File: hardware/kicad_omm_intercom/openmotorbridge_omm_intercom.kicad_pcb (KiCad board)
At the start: 2 copper layers, 60 x 30 mm, 19 parts, among them J1 TYPE-C-31-M-12_IP67, SW1 Power_MFB, SW2 Mesh_Group, SW3 Vol_Plus, SW4 Vol_Minus, U1 ESP32-C6-MINI-1U, U2 BQ24075RGTR, U3 XC6206P332MR, U4 ES8388, U5 ESP32-PICO-V3-02

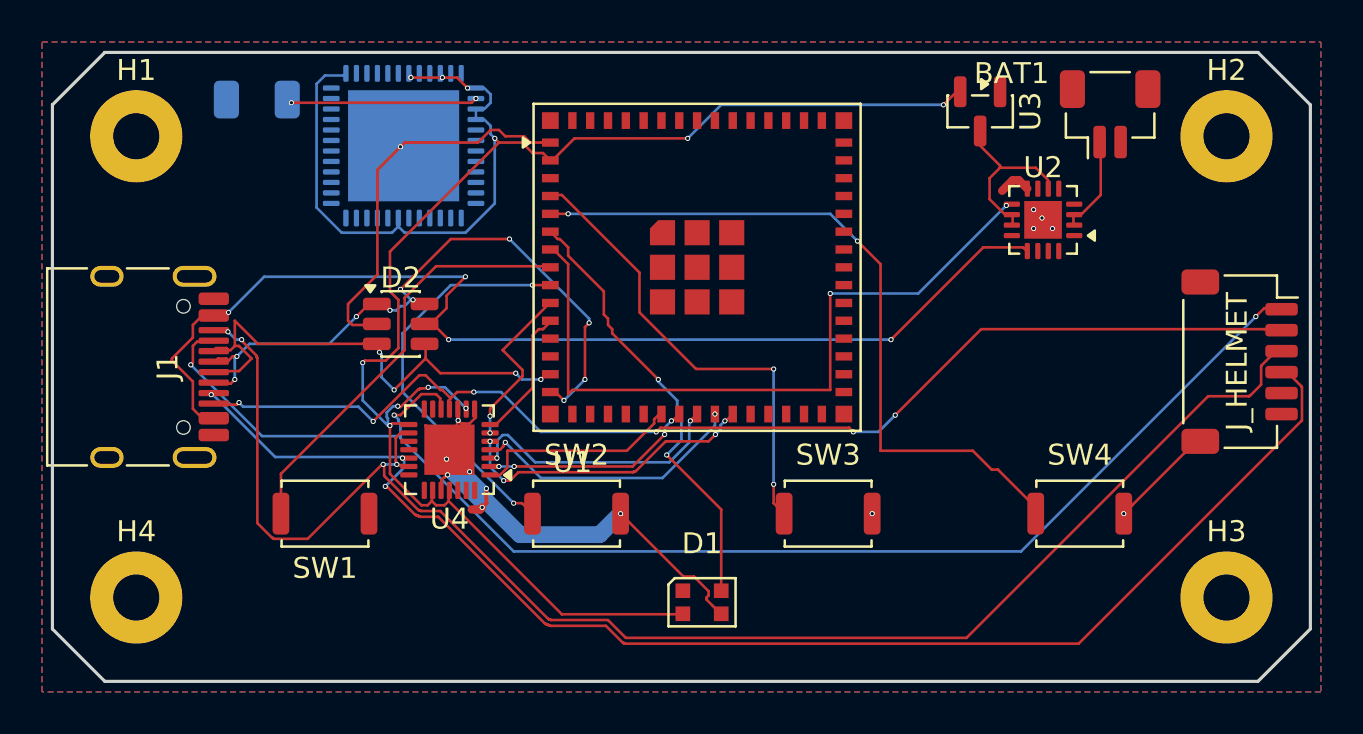
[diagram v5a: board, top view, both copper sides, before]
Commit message: hardware(omm): rotate J_HELMET by 180° inward, update CAD cutouts, CPL, gerbers, and docs
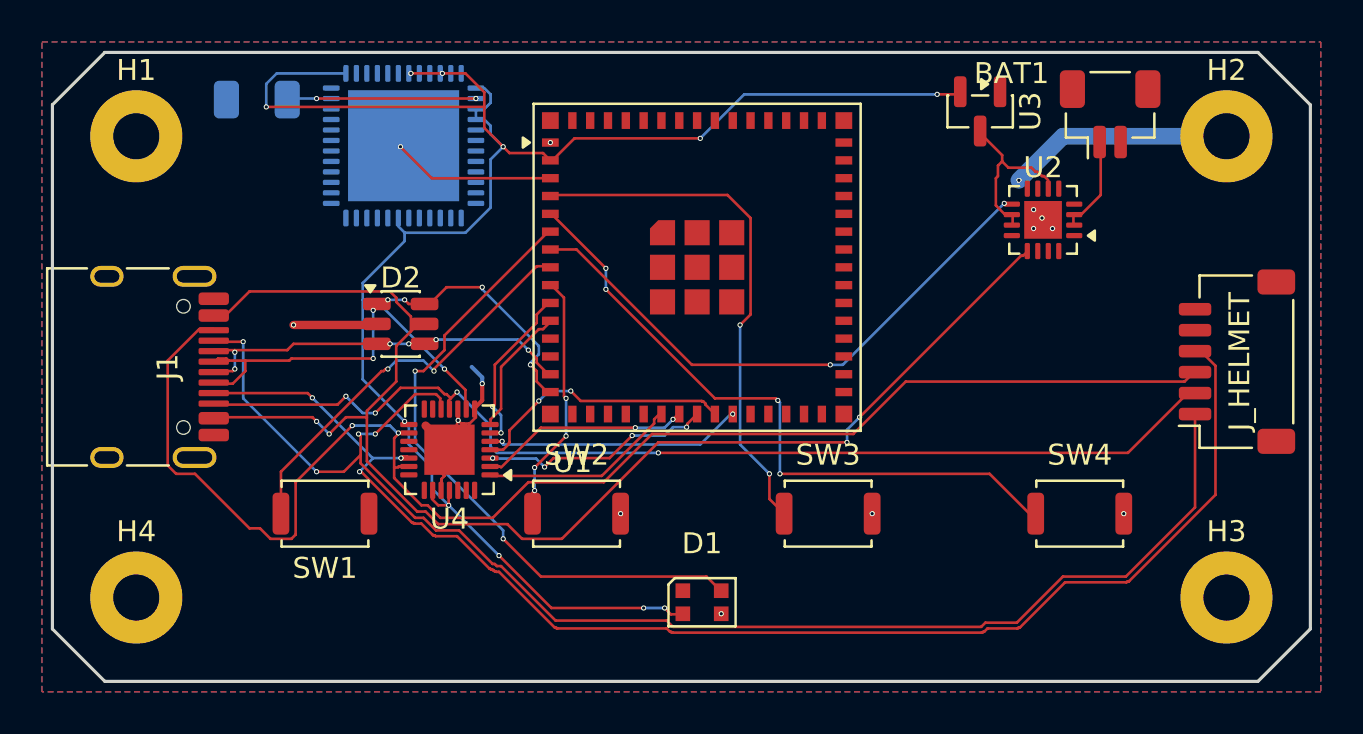
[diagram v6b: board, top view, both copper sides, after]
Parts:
- moved J_HELMET 0.12 mm to (126.5, 99.8), turned to 90 degrees
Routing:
- net GND: track 57.3 -> 38.3 mm
- net VBUS_5V: track 51.7 -> 65.2 mm
- net WS2812_DATA: track 20.9 -> 30.6 mm
- net BTN_MESH: track 19.5 -> 11.9 mm, vias 2 -> 4
- net CHG_STAT: track 34.5 -> 27.5 mm
- net USB_DP: track 29.4 -> 23.9 mm, vias 10 -> 6
- net USB_DN: track 23.5 -> 18.4 mm, vias 4 -> 6
- net AGND_SPK: track 73.7 -> 68.7 mm, vias 4 -> 2
- net HP_OUT_R: track 56.3 -> 51.4 mm, vias 6 -> 4
- net BTN_VOL_UP: track 22.3 -> 25.1 mm
- net BTN_VOL_DOWN: track 34.1 -> 31.7 mm, vias 2 -> 4
- net I2S_DIN: track 14.5 -> 12.5 mm, vias 4 -> 2
- net I2S_WS: track 12.5 -> 10.9 mm, vias 2 -> 4
- net HP_OUT_L: track 66.9 -> 68.1 mm, vias 3 -> 4
- net VCC_3V3: track 94.7 -> 95.8 mm, vias 11 -> 12
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
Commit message: feat(hw): finalize PCB lineup routing, sync PCBA 03 cartridge with J_PROG header and DTM12 schematics
- PCBA 01 (Central Box): Remediate net routing, DTM12 hierarchical schematic synchronization, 100% routed, 0 DRC errors.
- PCBA 03 (Smart Modular Cartridge): Position and route J_PROG 4-pin SMD programming header on F.Cu at (108.0, 89.61), synchronize CPL and schematic, 100% routed, 0 DRC errors.
- PCBA 05 (Universal Front Node): Preconnect and routing verified, 100% routed, 0 DRC errors.
- PCBA 07 (LoRa Smart-Keyfob): Routing and DRC verified, 100% routed, 0 DRC errors.
- PCBA 08 (Radar 2.0 Sub-MCU & Wings): Sub-MCU routing and HF isolation verified, 100% routed, 0 DRC errors.
- PCBA 10 (OMM 446 PMR/DMR Intercom): KiCad DRC verified, 100% routed, 0 DRC errors.
- Firmware: Align configuration headers across front_node and smart_cartridge.
- Tools: Add comprehensive preflight PCBA audit suite tools/audit_pcbas_preflight.py.
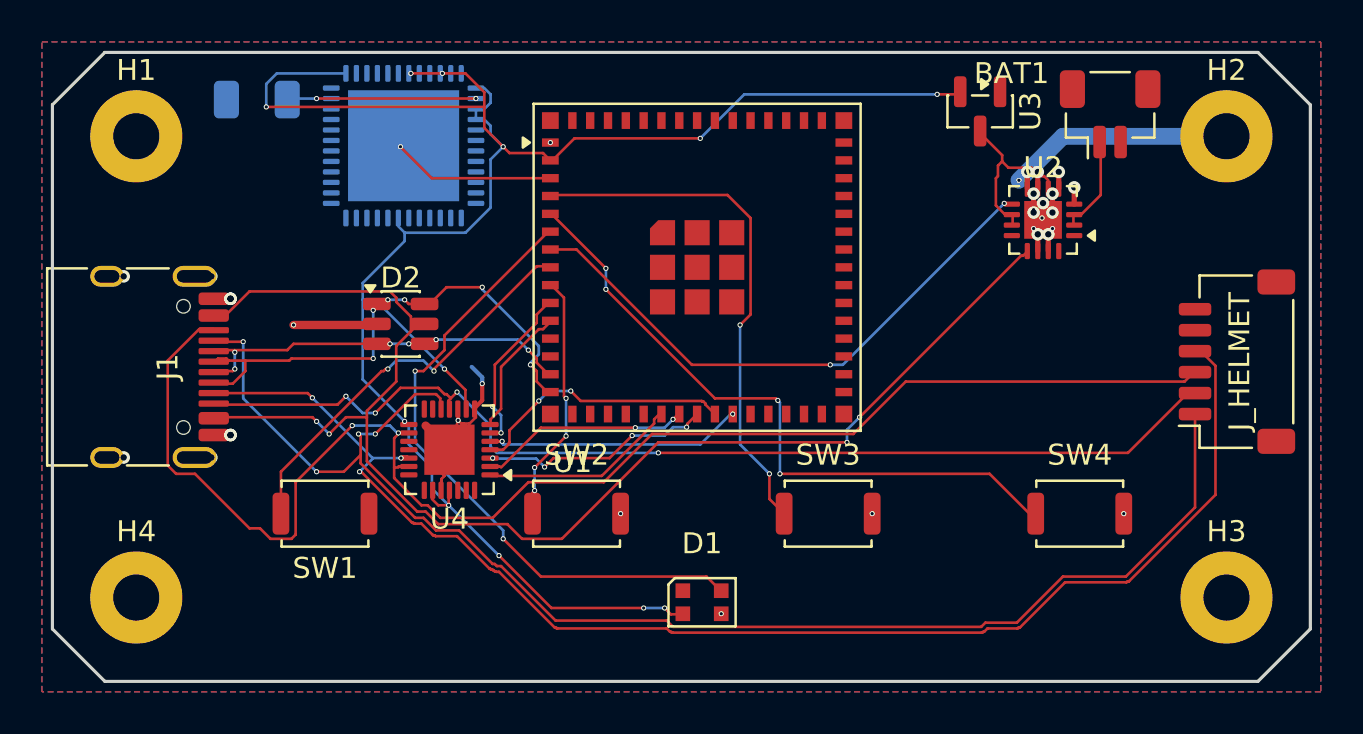
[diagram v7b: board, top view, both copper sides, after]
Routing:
- net GND: track 38.3 -> 53.5 mm, vias 14 -> 33
